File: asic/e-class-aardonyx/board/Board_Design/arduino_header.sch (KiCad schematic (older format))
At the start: 33 parts, among them J10 Conn_1x6, J11 Conn_1x6, J12 Conn_1x3_M, J13 Conn_1x8_F, J14 Conn_1x6_F, J15 Conn_1x10_F, J16 Conn_1x8_F, J19 Conn_1x3_M, J7 Conn_1x4, J8 Conn_1x3_M, J9 Conn_1x8, U5 CAT24M01WI-GT3, U6 IS25LP256x-xM, U7 ADC128S102CIMTX/NOPB, U8 LSF0108PWR, U9 LSF0108PWR

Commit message: Update layout
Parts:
- added C97: 1UF,0805, Capacitor_SMD:C_0805_2012Metric, symbol Aardonyx-rescue:C_Small-aardonyx
- added C98: 0.1UF,0402, Capacitor_SMD:C_0402_1005Metric, symbol Aardonyx-rescue:C_Small-aardonyx
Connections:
- net A8 is gone; now on net A7: J11.2 (Pin_2), U7.11 (IN7)
- net A7: no longer J11.1 (Pin_1), U7.10 (IN6)
- net AH_I2C1_SCL: now also J15.10 (Pin_10), U9.18 (B1); no longer J15.1 (Pin_1), U9.12 (B7)
- net AH_I2C1_SDA: now also J15.9 (Pin_9), U9.17 (B2); no longer J15.2 (Pin_2), U9.11 (B8)
- net AH_IO_0: now also J16.1 (Pin_1), U8.11 (B8); no longer J16.8 (Pin_8), U8.18 (B1)
- net AH_IO_1: now also J16.2 (Pin_2), U8.12 (B7); no longer J16.7 (Pin_7), U8.17 (B2)
- net AH_IO_10: now also J15.3 (Pin_3), U9.13 (B6); no longer J15.8 (Pin_8), U9.16 (B3)
- net AH_IO_11: now also J15.4 (Pin_4), U9.14 (B5); no longer J15.7 (Pin_7), U9.15 (B4)
- net AH_IO_12: now also J15.5 (Pin_5), U9.15 (B4); no longer J15.6 (Pin_6), U9.14 (B5)
- net AH_IO_13: now also J15.6 (Pin_6), U9.16 (B3); no longer J15.5 (Pin_5), U9.13 (B6)
- net AH_IO_2: now also J16.3 (Pin_3), U8.13 (B6); no longer J16.6 (Pin_6), U8.16 (B3)
- net AH_IO_3: now also J16.4 (Pin_4), U8.14 (B5); no longer J16.5 (Pin_5), U8.15 (B4)
- net AH_IO_4: now also J16.5 (Pin_5), U8.15 (B4); no longer J16.4 (Pin_4), U8.14 (B5)
- net AH_IO_5: now also J16.6 (Pin_6), U8.16 (B3); no longer J16.3 (Pin_3), U8.13 (B6)
- net AH_IO_6: now also J16.7 (Pin_7), U8.17 (B2); no longer J16.2 (Pin_2), U8.12 (B7)
- net AH_IO_7: now also J16.8 (Pin_8), U8.18 (B1); no longer J16.1 (Pin_1), U8.11 (B8)
- net AH_IO_8: now also J15.1 (Pin_1), U9.11 (B8); no longer J15.10 (Pin_10), U9.18 (B1)
- net AH_IO_9: now also J15.2 (Pin_2), U9.12 (B7); no longer J15.9 (Pin_9), U9.17 (B2)
- net GNDREF: now also J15.7 (Pin_7), C97.2, C98.2; no longer J15.4 (Pin_4)
- net I2C1_SCL: now also U9.3 (A1); no longer U9.9 (A7)
- net I2C1_SDA: now also U9.4 (A2); no longer U9.10 (A8)
- net IO_0: now also U8.10 (A8); no longer U8.3 (A1)
- net IO_1: now also U8.9 (A7); no longer U8.4 (A2)
- net IO_10: now also U9.8 (A6); no longer U9.5 (A3)
- net IO_11: now also U9.7 (A5); no longer U9.6 (A4)
- net IO_12: now also U9.6 (A4); no longer U9.7 (A5)
- net IO_13: now also U9.5 (A3); no longer U9.8 (A6)
- net IO_2: now also U8.8 (A6); no longer U8.5 (A3)
- net IO_3: now also U8.7 (A5); no longer U8.6 (A4)
- net IO_4: now also U8.6 (A4); no longer U8.7 (A5)
- net IO_5: now also U8.5 (A3); no longer U8.8 (A6)
- net IO_6: now also U8.4 (A2); no longer U8.9 (A7)
- net IO_7: now also U8.3 (A1); no longer U8.10 (A8)
- net IO_8: now also U9.10 (A8); no longer U9.3 (A1)
- net IO_9: now also U9.9 (A7); no longer U9.4 (A2)
- net V3P3: no longer J15.3 (Pin_3)
- net VAC: now also J15.8 (Pin_8)
- net VREF_AH: now also J13.2 (Pin_2)
- net V12P0: now reaches J13.8 (Pin_8)
- net V12P0: now also C97.1, C98.1
- new net A6: J11.1 (Pin_1), U7.10 (IN6)
- no-connect marks 3 -> 2

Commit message: Updating layout
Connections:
- net I2C0_SCL: now also J7.3 (Pin_3); no longer J7.2 (Pin_2)
- net I2C0_SDA: now also J7.2 (Pin_2); no longer J7.3 (Pin_3)
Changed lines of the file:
@@
 Text Notes 3650 4500 0    100  ~ 20
 SKT32E SPI - 8 CHANNEL \nADC INTERFACE\n
-Text HLabel 2300 7100 0    50   BiDi ~ 0
+Text HLabel 2300 7000 0    50   BiDi ~ 0
 I2C0_SDA
 Connection ~ 2150 1950
@@
 	4650 2150 4650 2250
 Wire Wire Line
-	2300 7000 2700 7000
-Wire Wire Line
-	2700 7100 2300 7100
+	2300 7100 2700 7100
+Wire Wire Line
+	2700 7000 2300 7000
 $Comp
 L Aardonyx-rescue:GND-aardonyx #PWR053
@@
 Text Label 2950 3300 0    39   ~ 0
 QSPI0_NCS_H
-Text HLabel 2300 7000 0    50   BiDi ~ 0
+Text HLabel 2300 7100 0    50   BiDi ~ 0
 I2C0_SCL
-Text Label 2300 7100 0    39   ~ 0
+Text Label 2300 7000 0    39   ~ 0
 I2C0_SDA
 Text Label 6650 5700 0    39   ~ 0
@@
 Wire Wire Line
 	6650 5500 7050 5500
-Text Label 2300 7000 0    39   ~ 0
+Text Label 2300 7100 0    39   ~ 0
 I2C0_SCL
 Text Label 2050 5550 0    39   ~ 0

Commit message: Updating layout
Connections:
- net A6: now also J11.4 (Pin_4); no longer J11.1 (Pin_1)
- net A7: now also J11.5 (Pin_5); no longer J11.2 (Pin_2)
- net I2C0_SCL: now also J7.2 (Pin_2); no longer J7.3 (Pin_3)
- net I2C0_SDA: now also J7.3 (Pin_3); no longer J7.2 (Pin_2)
- net IO_14: now also J11.2 (Pin_2); no longer J11.3 (Pin_3)
- net IO_15: now also J11.3 (Pin_3); no longer J11.4 (Pin_4)
- net V3P3: now also J11.1 (Pin_1); no longer J11.5 (Pin_5)
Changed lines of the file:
@@
 Text Notes 3650 4500 0    100  ~ 20
 SKT32E SPI - 8 CHANNEL \nADC INTERFACE\n
-Text HLabel 2300 7000 0    50   BiDi ~ 0
-I2C0_SDA
 Connection ~ 2150 1950
 Connection ~ 1900 2050
@@
 Wire Wire Line
 	4650 2150 4650 2250
-Wire Wire Line
-	2300 7100 2700 7100
-Wire Wire Line
-	2700 7000 2300 7000
 $Comp
 L Aardonyx-rescue:GND-aardonyx #PWR053
@@
 Wire Wire Line
 	2650 6900 2700 6900
-Wire Wire Line
-	4300 1850 4700 1850
-Wire Wire Line
-	4300 1550 4700 1550
-Text Label 4300 1550 0    39   ~ 0
-QSPI0_CLK
 Text HLabel 1250 1750 0    50   BiDi ~ 0
 QSPI0_IO0
@@
 Text HLabel 2950 3100 0    50   Input ~ 0
 QSPI0_NCS
-Text Label 4300 1650 0    39   ~ 0
-QSPI0_IO0
-Wire Wire Line
-	4700 1650 4300 1650
 Text Label 2950 3100 0    39   ~ 0
 QSPI0_NCS
@@
 Text Label 2950 3300 0    39   ~ 0
 QSPI0_NCS_H
-Text HLabel 2300 7100 0    50   BiDi ~ 0
-I2C0_SCL
-Text Label 2300 7000 0    39   ~ 0
-I2C0_SDA
-Text Label 6650 5700 0    39   ~ 0
+Text Label 6650 5600 0    39   ~ 0
 IO_15
-Text Label 6650 5600 0    39   ~ 0
+Text Label 6650 5500 0    39   ~ 0
+IO_14
+Text HLabel 6650 5500 0    50   BiDi ~ 0
 IO_14
 Text HLabel 6650 5600 0    50   BiDi ~ 0
-IO_14
-Text HLabel 6650 5700 0    50   BiDi ~ 0
 IO_15
 Wire Wire Line
+	6650 5500 7050 5500
+Wire Wire Line
 	6650 5600 7050 5600
-Wire Wire Line
-	6650 5700 7050 5700
 Wire Wire Line
 	7050 4900 6850 4900
@@
 $EndComp
 Wire Wire Line
-	6650 6050 6850 6050
-Wire Wire Line
-	6850 6050 6850 5800
-Wire Wire Line
-	6850 5800 7050 5800
-Wire Wire Line
 	7050 5900 6900 5900
 Wire Wire Line
@@
 	1    0    0    -1
 $EndComp
-Text Label 6650 5400 0    50   ~ 0
+Text Label 6650 5700 0    50   ~ 0
 A6
-Text Label 6650 5500 0    50   ~ 0
+Text Label 6650 5800 0    50   ~ 0
 A7
 Wire Wire Line
-	6650 5400 7050 5400
-Wire Wire Line
-	6650 5500 7050 5500
-Text Label 2300 7100 0    39   ~ 0
-I2C0_SCL
+	6650 5700 7050 5700
+Wire Wire Line
+	6650 5800 7050 5800
 Text Label 2050 5550 0    39   ~ 0
 I2C0_SCL
 Text Label 2050 5750 0    39   ~ 0
 I2C0_SDA
-Wire Wire Line
-	4300 1950 4700 1950
-Wire Wire Line
-	4300 2050 4700 2050
-Wire Wire Line
-	4300 1750 4700 1750
-Text Label 4300 1750 0    39   ~ 0
-QSPI0_IO1
-Text Label 4300 1850 0    39   ~ 0
-QSPI0_IO2
-Text Label 4300 2050 0    39   ~ 0
-QSPI0_NCS_H
-Text Label 4300 1950 0    39   ~ 0
-QSPI0_IO3
 Text Label 3650 1750 2    39   ~ 0
 QSPI0_IO1
@@
 L Aardonyx-rescue:V3P3 #PWR?
 U 1 1 5F2908DF
-P 6650 5950
+P 6650 5300
 AR Path="/5D8B3761/5F2908DF" Ref="#PWR?"  Part="1"
 AR Path="/5D8B37DE/5F2908DF" Ref="#PWR0181"  Part="1"
-F 0 "#PWR0181" H 6800 5900 50  0001 C CNN
-F 1 "V3P3" H 6655 6123 50  0000 C CNN
-F 2 "" H 6650 5950 50  0001 C CNN
-F 3 "" H 6650 5950 50  0001 C CNN
-	1    6650 5950
-	1    0    0    -1
-$EndComp
-Wire Wire Line
-	6650 6050 6650 5950
+F 0 "#PWR0181" H 6800 5250 50  0001 C CNN
+F 1 "V3P3" H 6655 5473 50  0000 C CNN
+F 2 "" H 6650 5300 50  0001 C CNN
+F 3 "" H 6650 5300 50  0001 C CNN
+	1    6650 5300
+	1    0    0    -1
+$EndComp
+Wire Wire Line
+	6650 5400 6650 5300
 $Comp
 L Aardonyx-rescue:V3P3 #PWR?
@@
 	7750 5150 7750 5400
 Connection ~ 8100 5400
+Wire Wire Line
+	6650 5400 7050 5400
+Text Label 4300 1950 0    39   ~ 0
+QSPI0_IO3
+Text Label 4300 2050 0    39   ~ 0
+QSPI0_NCS_H
+Text Label 4300 1850 0    39   ~ 0
+QSPI0_IO2
+Text Label 4300 1750 0    39   ~ 0
+QSPI0_IO1
+Wire Wire Line
+	4300 1750 4700 1750
+Wire Wire Line
+	4300 2050 4700 2050
+Wire Wire Line
+	4300 1950 4700 1950
+Wire Wire Line
+	4700 1650 4300 1650
+Text Label 4300 1650 0    39   ~ 0
+QSPI0_IO0
+Text Label 4300 1550 0    39   ~ 0
+QSPI0_CLK
+Wire Wire Line
+	4300 1550 4700 1550
+Wire Wire Line
+	4300 1850 4700 1850
+Text Label 2300 7100 0    39   ~ 0
+I2C0_SDA
+Wire Wire Line
+	2700 7100 2300 7100
+Text HLabel 2300 7100 0    50   BiDi ~ 0
+I2C0_SDA
+Text Label 2300 7000 0    39   ~ 0
+I2C0_SCL
+Text HLabel 2300 7000 0    50   BiDi ~ 0
+I2C0_SCL
+Wire Wire Line
+	2300 7000 2700 7000
 Wire Bus Line
 	8650 2550 8650 3100

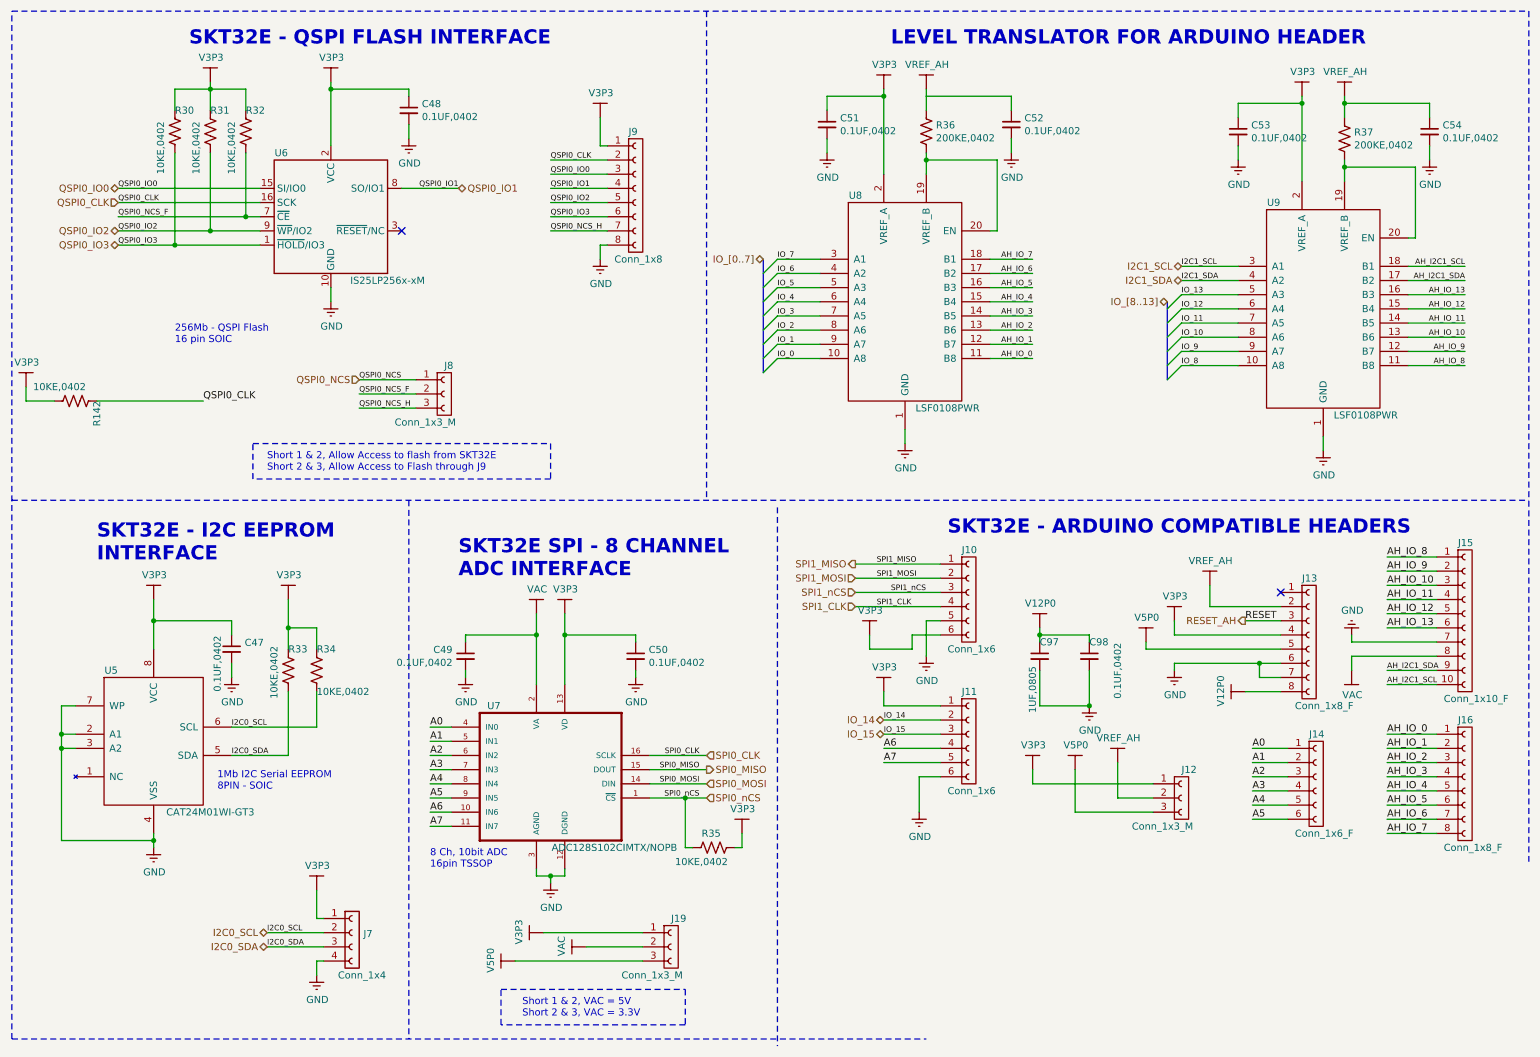
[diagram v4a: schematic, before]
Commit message: Updating layout after back annotation
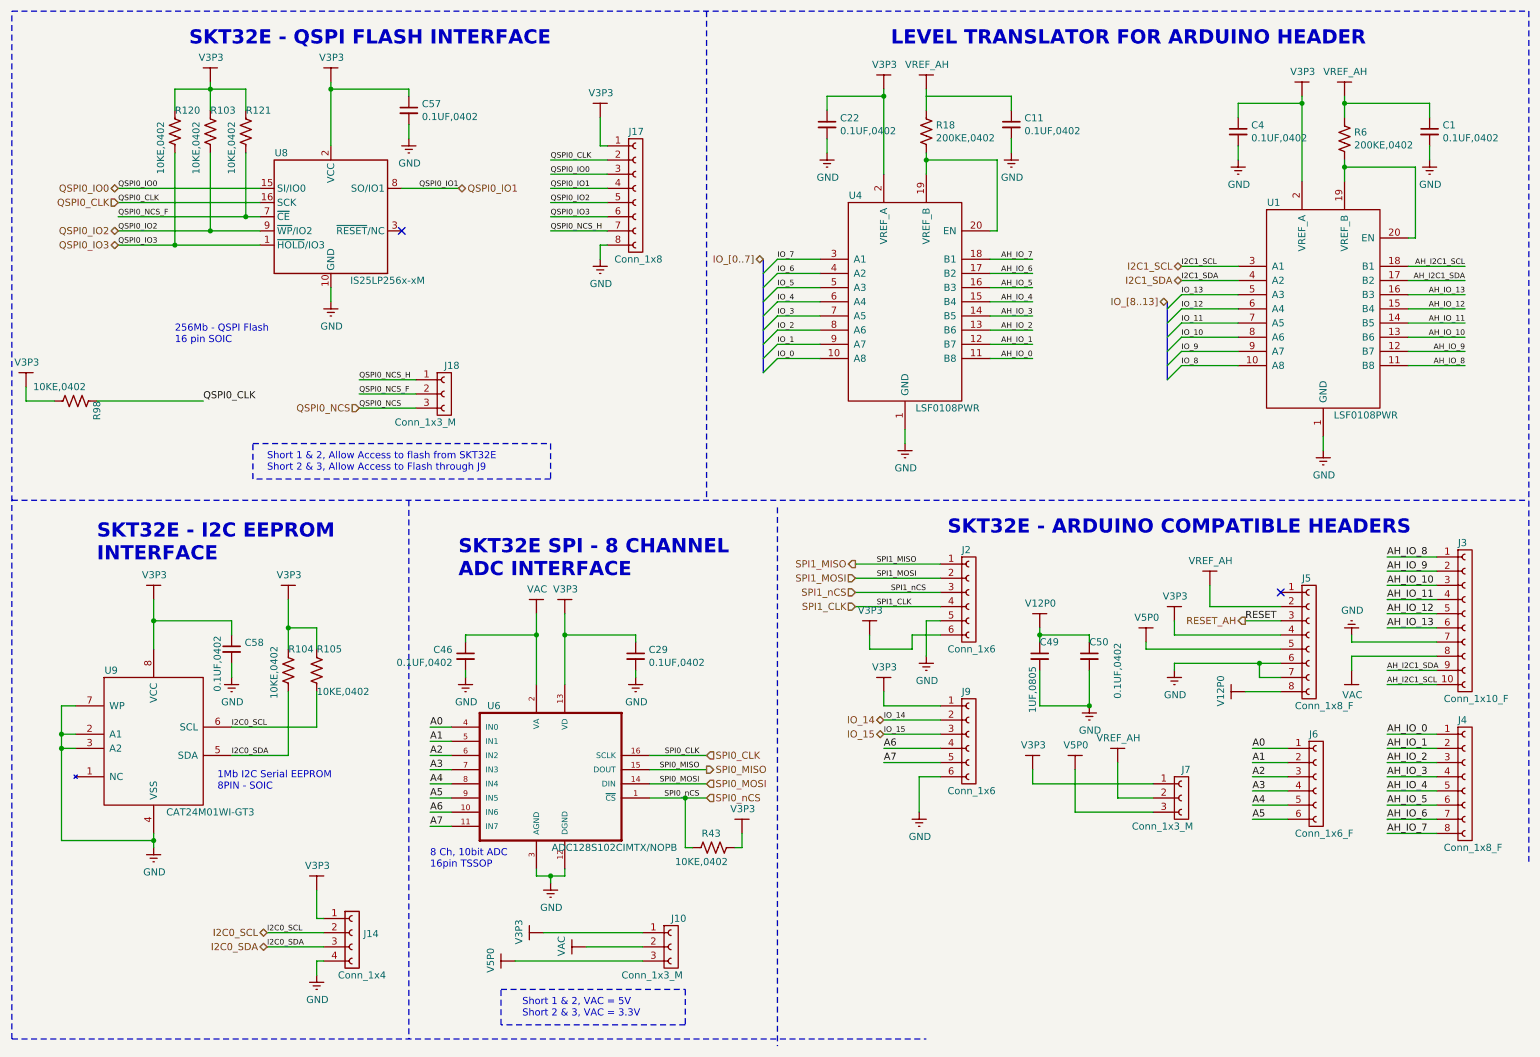
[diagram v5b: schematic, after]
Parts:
- renumbered C54 to C1, C52 to C11, C51 to C22, C50 to C29, C53 to C4, C49 to C46, C97 to C49, C98 to C50, C48 to C57, C47 to C58, J19 to J10, J7 to J14, J9 to J17, J8 to J18, J10 to J2, J15 to J3, J16 to J4, J13 to J5, J14 to J6, J12 to J7, J11 to J9, R31 to R103, R33 to R104, R34 to R105, R30 to R120, R32 to R121, R36 to R18, R35 to R43, R37 to R6, R142 to R98, U9 to U1, U8 to U4, U7 to U6, U6 to U8, U5 to U9
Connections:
- net QSPI0_NCS: now also J18.3 (Pin_3); no longer J18.1 (Pin_1)
- net QSPI0_NCS_H: now also J18.1 (Pin_1); no longer J18.3 (Pin_3)
